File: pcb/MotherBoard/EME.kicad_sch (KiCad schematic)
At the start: 48 parts, among them J1 BMP180, J10 Reset, J11 UART2, J12 SPI_CONN, J13 UART0, J14 MQ135, J15 5v, J16 GPIO's, J17 Anemómetro, J19 I2C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

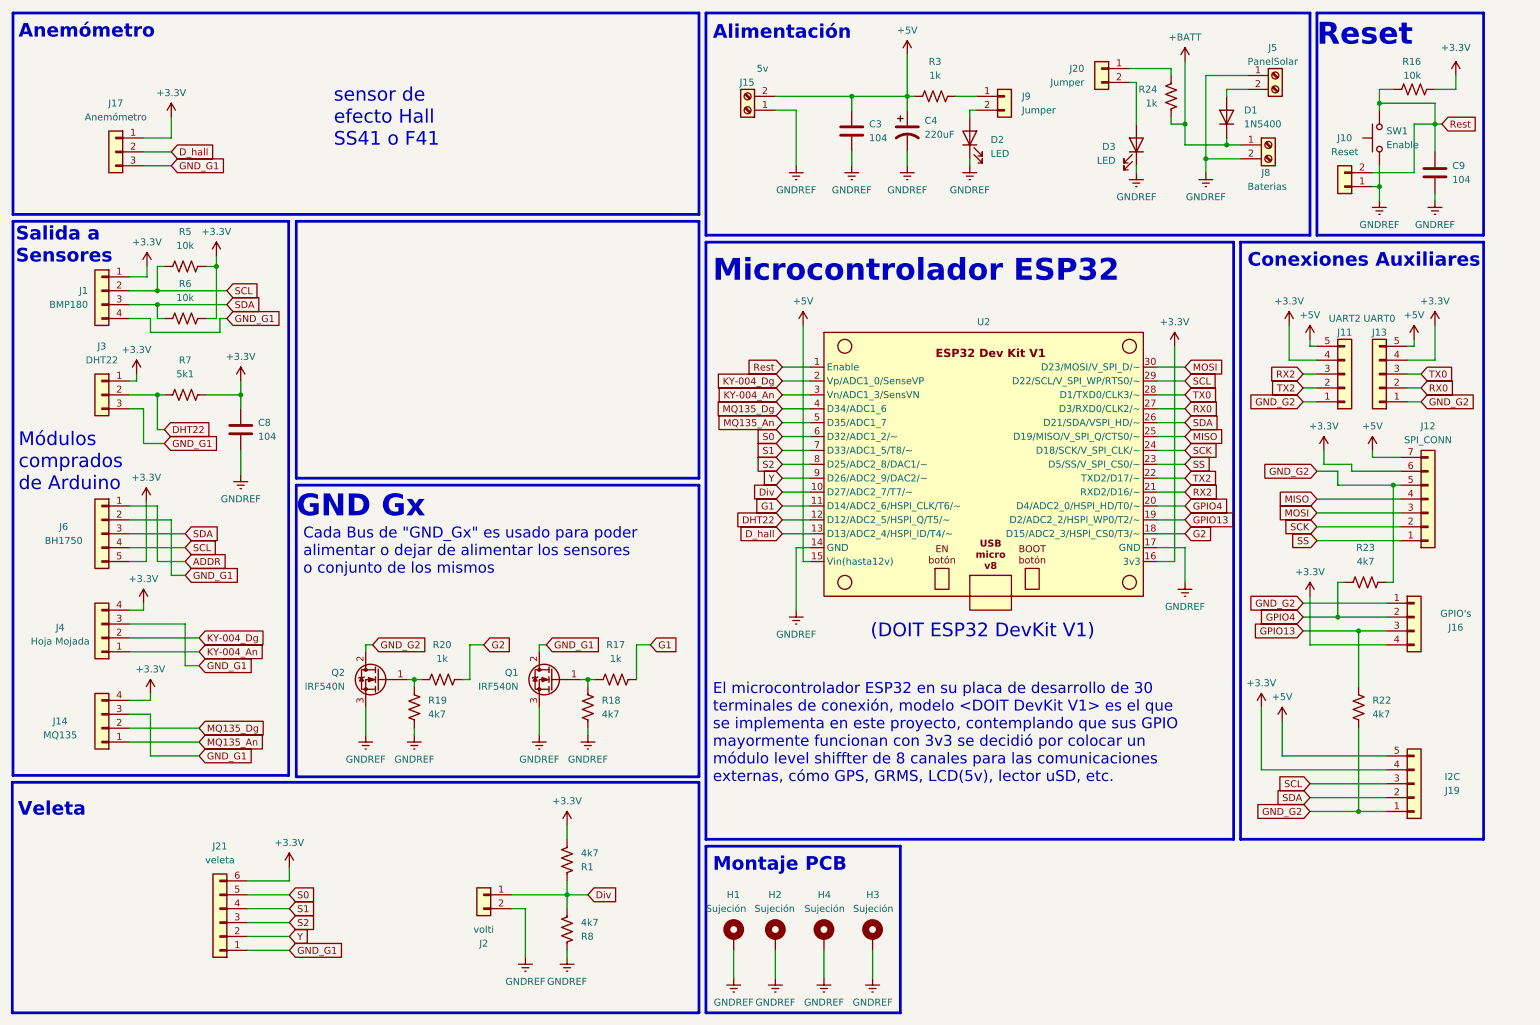
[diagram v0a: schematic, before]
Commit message: se readaptaron y revisaron las PCBs, listas para imprimir
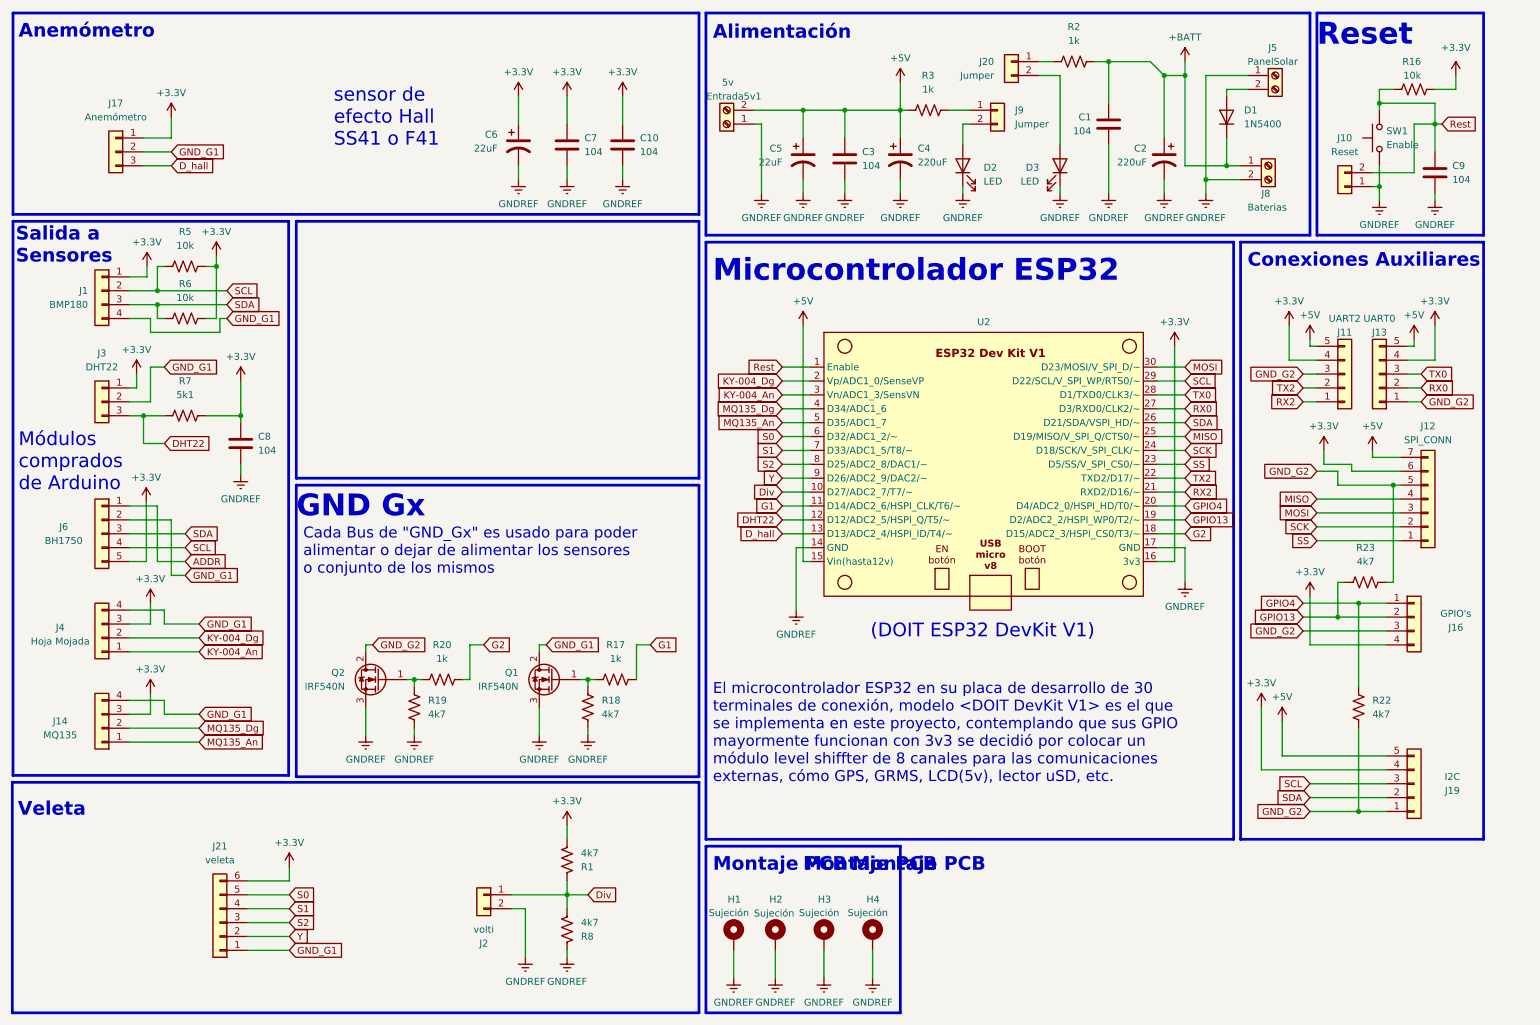
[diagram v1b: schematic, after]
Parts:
- removed H1, H2, H3, H4: Sujeción, MountingHole:MountingHole_3.2mm_M3_Pad_Via, symbol Mechanical:MountingHole_Pad_MP
- removed R24: 1k, Resistor_THT:R_Axial_DIN0207_L6.3mm_D2.5mm_P10.16mm_Horizontal, symbol Device:R_US
- added C1, C10, C7: 104, Capacitor_THT:C_Disc_D7.0mm_W2.5mm_P5.00mm, symbol Device:C
- added C2: 220uF, Capacitor_THT:C_Radial_D8.0mm_H11.5mm_P3.50mm, symbol Device:C_Polarized_US
- added C5, C6: 22uF, Capacitor_THT:C_Radial_D8.0mm_H7.0mm_P3.50mm, symbol Device:C_Polarized_US
- added H1, H2, H3, H4: Sujeción, MountingHole:MountingHole_3.5mm_Pad, symbol Mechanical:MountingHole_Pad
- added R2: 1k, Resistor_THT:R_Axial_DIN0207_L6.3mm_D2.5mm_P10.16mm_Horizontal, symbol Device:R_US
- C3: footprint Capacitor_THT:C_Disc_D4.3mm_W1.9mm_P5.00mm -> Capacitor_THT:C_Disc_D7.0mm_W2.5mm_P5.00mm
- C8: footprint Capacitor_THT:C_Disc_D4.3mm_W1.9mm_P5.00mm -> Capacitor_THT:C_Disc_D7.5mm_W4.4mm_P5.00mm
- renumbered J15 to Entrada5v1
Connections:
- net +3.3V: now also J14.3 (Pin_3), J4.3 (Pin_3), C10.1, C6.1, C7.1; no longer J14.4 (Pin_4), J4.4 (Pin_4)
- net +5V: now also C5.1
- net +BATT: now also C1.1, C2.1, R2.2
- net DHT22: now also J3.3 (Pin_3); no longer J3.2 (Pin_2)
- net D_hall: now also J17.3 (Pin_3); no longer J17.2 (Pin_2)
- net GNDREF: now also C1.2, C10.2, C2.2, C5.2, C6.2, C7.2, H1.1, H2.1, H3.1, H4.1
- net GND_G1: now also J14.4 (Pin_4), J17.2 (Pin_2), J3.2 (Pin_2), J4.4 (Pin_4); no longer J14.3 (Pin_3), J17.3 (Pin_3), J3.3 (Pin_3), J4.3 (Pin_3)
- net GND_G2: now also J11.3 (Pin_3), J16.3 (Pin_3); no longer J11.1 (Pin_1), J16.1 (Pin_1)
- net GPIO13: now also J16.2 (Pin_2), R23.2; no longer J16.3 (Pin_3), R22.2
- net GPIO4: now also J16.1 (Pin_1), R22.2; no longer J16.2 (Pin_2), R23.2
- net RX2: now also J11.1 (Pin_1); no longer J11.3 (Pin_3)
- net at J20.1 (Pin_1): now also R2.1
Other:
- moved on the sheet: C3, C4, C8, D2, D3, Entrada5v1, J20, J3, J8, J9, R3, R7

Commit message: Se agregó la modificación del MQ135 a 5v con divisor resistivo; además de cambio del DHT del pin 12; también se modificaron los pines de conexión
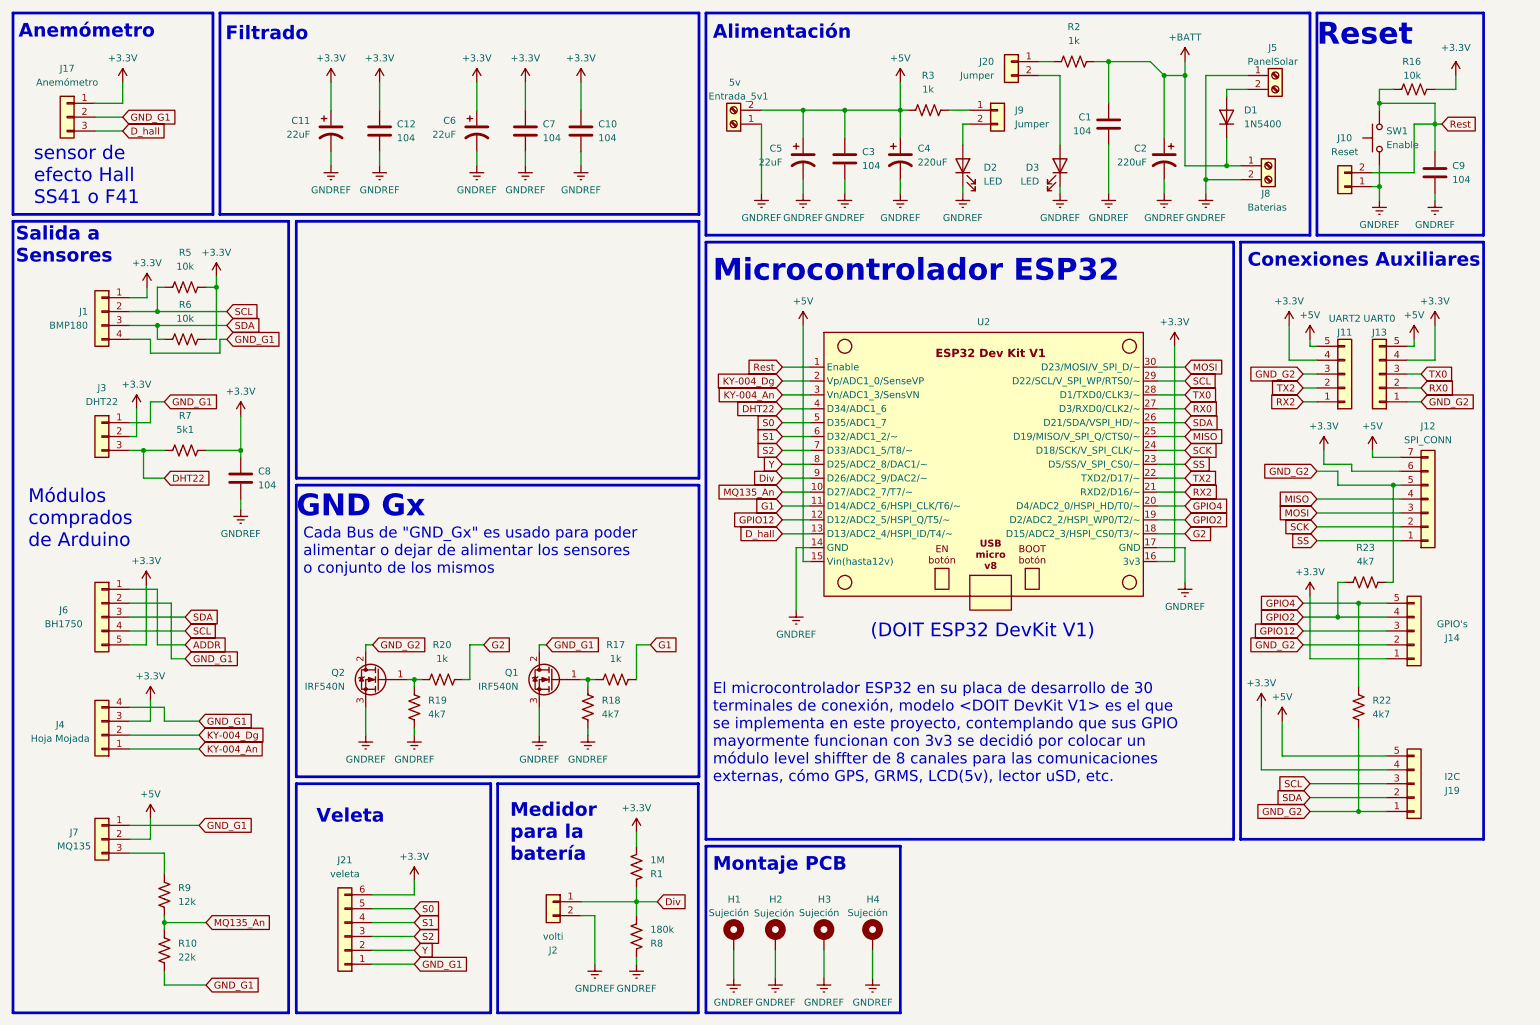
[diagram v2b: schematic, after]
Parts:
- removed J14: MQ135, Connector_PinHeader_2.54mm:PinHeader_1x04_P2.54mm_Vertical, symbol Connector_Generic:Conn_01x04
- removed J16: GPIO's, Connector_PinHeader_2.54mm:PinHeader_1x04_P2.54mm_Vertical, symbol Connector_Generic:Conn_01x04
- added C11: 22uF, Capacitor_THT:C_Radial_D8.0mm_H7.0mm_P3.50mm, symbol Device:C_Polarized_US
- added C12: 104, Capacitor_THT:C_Disc_D7.0mm_W2.5mm_P5.00mm, symbol Device:C
- added J14: GPIO's, Connector_PinHeader_2.54mm:PinHeader_1x05_P2.54mm_Vertical, symbol Connector_Generic:Conn_01x05
- added J7: MQ135, Connector_PinHeader_2.54mm:PinHeader_1x03_P2.54mm_Vertical, symbol Connector_Generic:Conn_01x03
- added R10: 22k, Resistor_THT:R_Axial_DIN0207_L6.3mm_D2.5mm_P10.16mm_Horizontal, symbol Device:R_US
- added R9: 12k, Resistor_THT:R_Axial_DIN0207_L6.3mm_D2.5mm_P10.16mm_Horizontal, symbol Device:R_US
- R1: value 4k7 -> 1M
- R8: value 4k7 -> 180k
- renumbered Entrada5v1 to Entrada_5v1
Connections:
- net MQ135_Dg is gone; now on net DHT22: U2.4 (D34/ADC1_6)
- net +3.3V: now also J3.2 (Pin_2), C11.1, C12.1, J14.1 (Pin_1); no longer J3.1 (Pin_1)
- net +5V: now also J7.2 (Pin_2)
- net DHT22: no longer U2.12 (D12/ADC2_5/HSPI_Q/T5/~)
- net Div: now also U2.9 (D26/ADC2_9/DAC2/~); no longer U2.10 (D27/ADC2_7/T7/~)
- net GNDREF: now also C11.2, C12.2
- net GND_G1: now also J3.1 (Pin_1), J7.1 (Pin_1), R10.1; no longer J3.2 (Pin_2)
- net GND_G2: now also J14.2 (Pin_2)
- net GPIO4: now also J14.5 (Pin_5)
- net MQ135_An: now also U2.10 (D27/ADC2_7/T7/~), R10.2, R9.1; no longer U2.5 (D35/ADC1_7)
- net S0: now also U2.5 (D35/ADC1_7); no longer U2.6 (D32/ADC1_2/~)
- net S1: now also U2.6 (D32/ADC1_2/~); no longer U2.7 (D33/ADC1_5/T8/~)
- net S2: now also U2.7 (D33/ADC1_5/T8/~); no longer U2.8 (D25/ADC2_8/DAC1/~)
- net Y: now also U2.8 (D25/ADC2_8/DAC1/~); no longer U2.9 (D26/ADC2_9/DAC2/~)
- net GPIO13 renamed GPIO2
- net GPIO2: now also J14.4 (Pin_4)
- new net: J7.3 (Pin_3), R9.2
- new net GPIO12: J14.3 (Pin_3), U2.12 (D12/ADC2_5/HSPI_Q/T5/~)
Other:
- note added: "Filtrado"
- note added: "Medidor para la batería"
- moved on the sheet: C10, C6, C7, C8, Entrada_5v1, J1, J17, J2, J21, J3, J4, J6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
